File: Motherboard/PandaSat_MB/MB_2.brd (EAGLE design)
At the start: 93.9 x 89.2 mm, 164 parts, among them J1 503182-1852, J14 M023.5MM_LOCK, J15 M023.5MM_LOCK, J16 M023.5MM_LOCK, J2 10118194-0001LF, J3 DCJ0303, J4 BU-SMA-V, J5 BK-18650, K4 PE014006, Q1 IRLML2803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

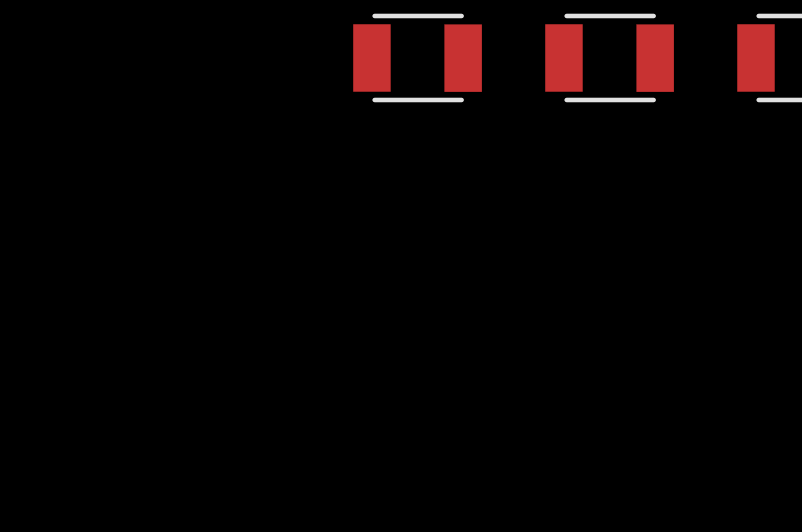
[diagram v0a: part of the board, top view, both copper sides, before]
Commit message: Added USB Bypass
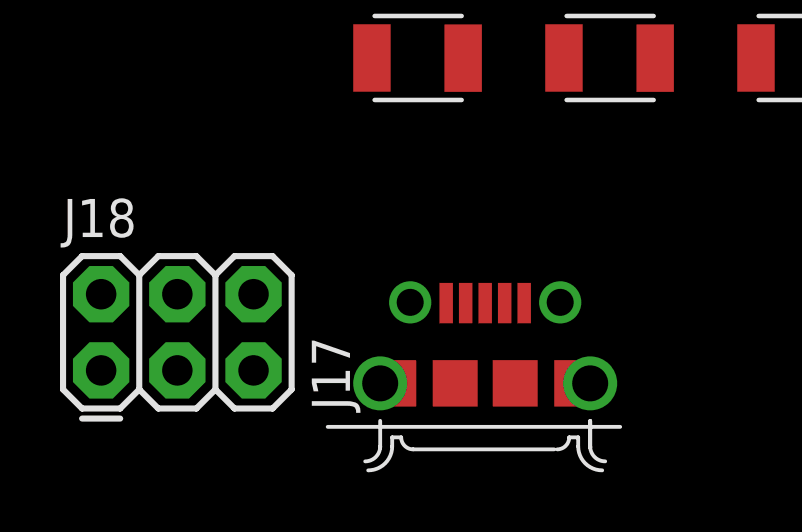
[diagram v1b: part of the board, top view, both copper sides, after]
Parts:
- added J17: 10118194-0001LF, 10118194-0001LF:FRAMATOME_10118194-0001LF
- added J18: (no value), SparkFun-Connectors:2X3
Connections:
- new net N$22: J17.3, J18.2
- new net N$40: J17.2, J18.4
- new net N$42: J17.1, J18.1
- new net N$57: J17.5, J18.5
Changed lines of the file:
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@@
 <attribute name="VALUE" x="-223.7434" y="-21.4674" size="1" layer="27"/>
+</element>
+<element name="J17" library="10118194-0001LF" package="FRAMATOME_10118194-0001LF" value="10118194-0001LF" x="-218.0082" y="-29.4132" smashed="yes">
+<attribute name="AVAILABILITY" value="Warning" x="-218.0082" y="-29.4132" size="1.778" layer="27" display="off"/>
+<attribute name="DESCRIPTION" value=" Micro Usb, 2.0 Type b, Rcpt, Smt " x="-218.0082" y="-29.4132" size="1.778" layer="27" display="off"/>
+<attribute name="MF" value="Amphenol" x="-218.0082" y="-29.4132" size="1.778" layer="27" display="off"/>
+<attribute name="MP" value="10118194-0001LF" x="-218.0082" y="-29.4132" size="1.778" layer="27" display="off"/>
+<attribute name="NAME" x="-222.5159" y="-30.314740625" size="1.27218125" layer="25" rot="R90"/>
+<attribute name="PACKAGE" value="None" x="-218.0082" y="-29.4132" size="1.778" layer="27" display="off"/>
+<attribute name="PRICE" value="0.26 USD" x="-218.0082" y="-29.4132" size="1.778" layer="27" display="off"/>
+<attribute name="VALUE" x="-212.099059375" y="-29.313046875" size="1.271959375" layer="27" rot="R90"/>
+</element>
+<element name="J18" library="SparkFun-Connectors" package="2X3" value="" x="-230.8098" y="-28.9814" smashed="yes">
+<attribute name="NAME" x="-232.0798" y="-24.5364" size="1.27" layer="25" ratio="10"/>
+<attribute name="VALUE" x="-232.0798" y="-32.1564" size="1.27" layer="27"/>
 </element>
 </elements>
@@
 <wire x1="-51.665" y1="32.451" x2="-212.3426" y2="-18.5724" width="0" layer="19" extent="1-1"/>
 </signal>
+<signal name="N$22">
+<contactref element="J17" pad="3"/>
+<contactref element="J18" pad="2"/>
+<wire x1="-230.8098" y1="-26.4414" x2="-218.0082" y2="-26.7382" width="0" layer="19" extent="1-1"/>
+</signal>
+<signal name="N$40">
+<contactref element="J17" pad="2"/>
+<contactref element="J18" pad="4"/>
+<wire x1="-218.6582" y1="-26.7382" x2="-228.2698" y2="-26.4414" width="0" layer="19" extent="1-1"/>
+</signal>
+<signal name="N$42">
+<contactref element="J17" pad="1"/>
+<contactref element="J18" pad="1"/>
+<wire x1="-230.8098" y1="-28.9814" x2="-219.3082" y2="-26.7382" width="0" layer="19" extent="1-1"/>
+</signal>
+<signal name="N$57">
+<contactref element="J17" pad="5"/>
+<contactref element="J18" pad="5"/>
+<wire x1="-216.7082" y1="-26.7382" x2="-225.7298" y2="-28.9814" width="0" layer="19" extent="1-1"/>
+</signal>
 </signals>

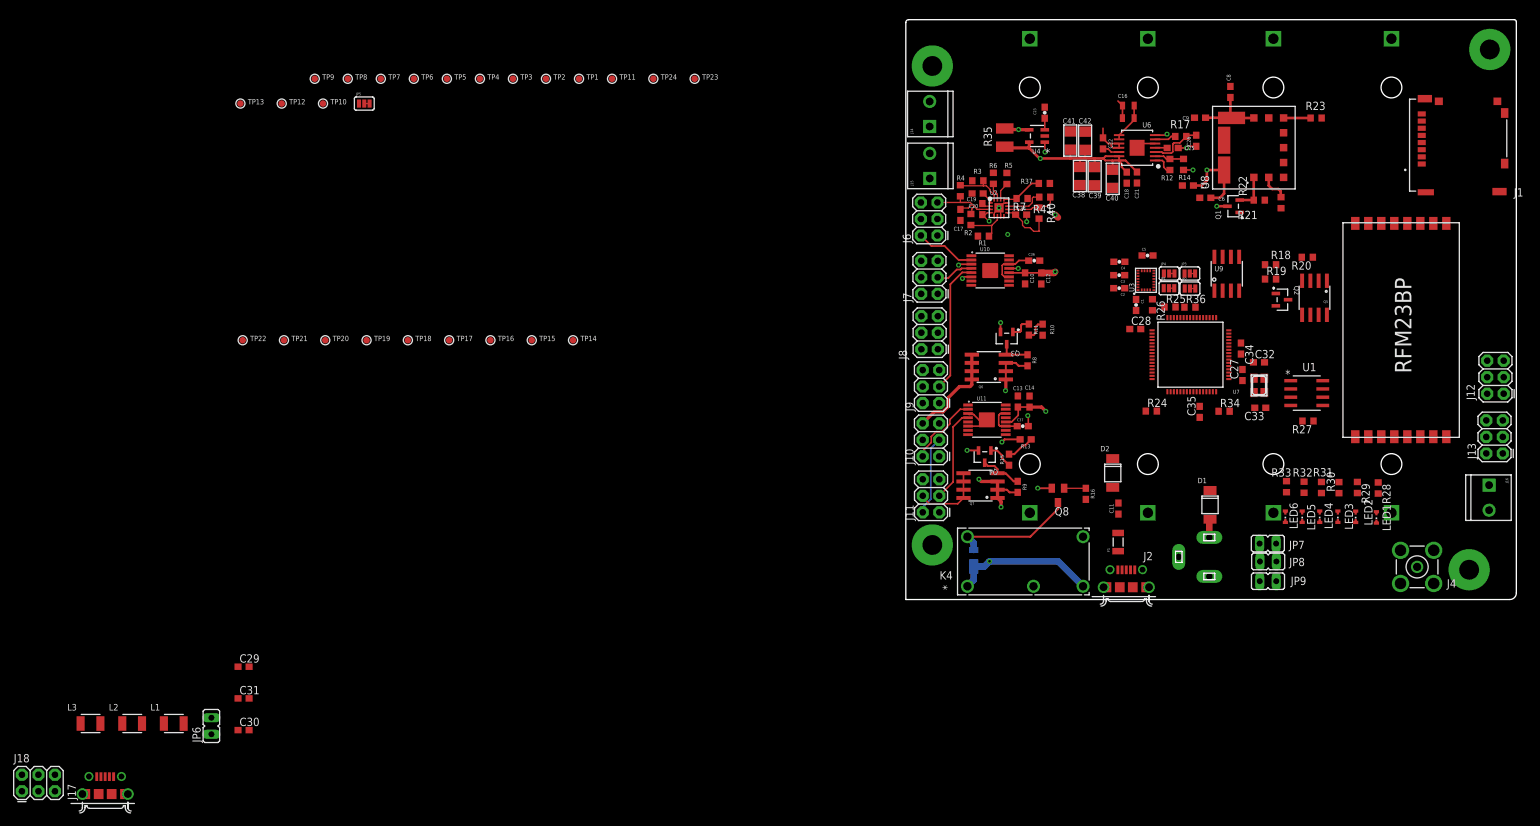
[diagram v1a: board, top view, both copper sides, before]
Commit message: Switched Barrel Jack to smd Changed Footprints for 2x3 conn to include casing Changed Hbridges to pair x&z instead of x&y fixed mislabeled net PL_PWR_EN -> PL_PWR_ENAB
Did all the signal routing, just need 5V and 3.3V
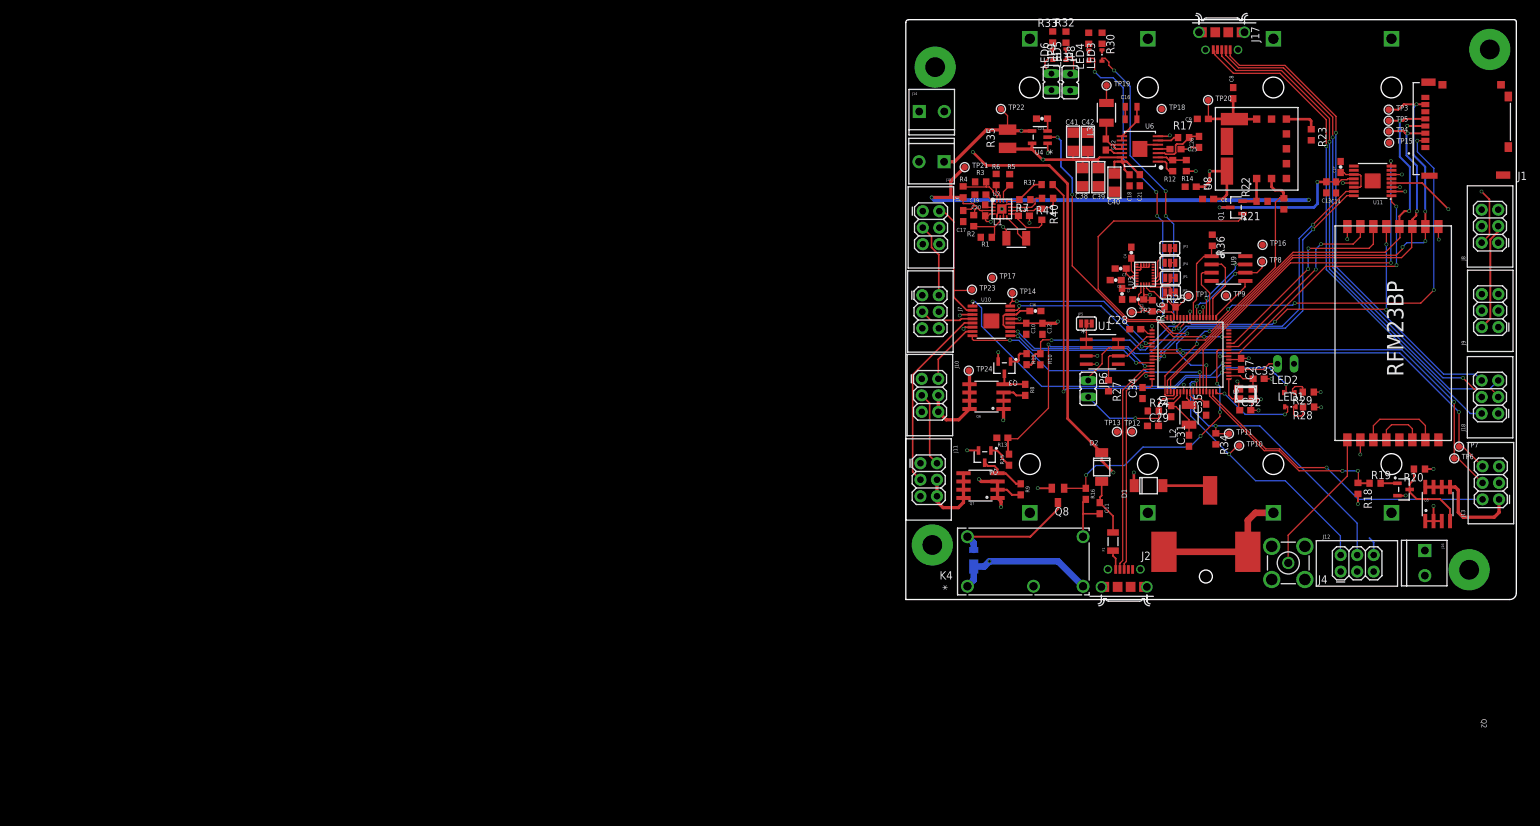
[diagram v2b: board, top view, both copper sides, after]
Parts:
- J10, J11, J12, J13, J18, J6, J7, J8, J9: device SparkFun-Connectors:2X3 -> pandasat:2X3
- J3: value DCJ0303 -> PJ-036AH-SMT-TRSMD; device maholli:DCJ0303 -> pandasat:BARRELJACK_5.0MMX2.1MM_SMD
- moved J18 234.3 mm to (-3.78, 29.1), turned to 90 degrees
- moved J17 207.9 mm to (-46.3, 87.7), turned to 180 degrees
- moved L3 182.3 mm to (-64.0, 75.4), turned to 90 degrees
- moved TP7 175.2 mm to (-9.81, 24.0)
- moved TP6 170.3 mm to (-10.5, 22.2)
- moved L2 169.3 mm to (-51.3, 28.9), turned to 90 degrees
- moved C30 150.8 mm to (-54.1, 29.5), turned to 90 degrees
- moved C31 150.7 mm to (-51.3, 24.9), turned to 90 degrees
- moved TP10 150.4 mm to (-43.6, 24.2)
- moved L1 149.5 mm to (-77.9, 56.1)
- moved TP5 145.0 mm to (-20.6, 74.1)
- moved C29 144.7 mm to (-56.9, 27.2)
- moved JP6 144.5 mm to (-66.8, 32.9), turned to 180 degrees
- moved TP9 144.0 mm to (-45.6, 47.2)
- moved TP13 143.9 mm to (-62.4, 26.3)
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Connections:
- net DXY_FAULT renamed DXZ_FAULT
- net DZ_FAULT renamed DY_FAULT
- net MXY_EN renamed MXZ_EN
- net MZ_EN renamed MY_EN
- removed net N$57: J17.5, J18.5
- removed net PL_PWR_EN: U7.62
- new net N$59: J16.1, J3.P$2, J3.P$3, J5.1, J5.2
- new net N$63: J7.6
- new net N$64: J7.4
- new net N$65: J8.6
- new net N$66: J8.4
- new net N$67: J9.6
- new net N$68: J9.4
- net MINY_1: now also U11.16; no longer U10.9
- net MINY_2: now also U11.15; no longer U10.10
- net MINZ_1: now also U10.9; no longer U11.16
- net MINZ_2: now also U10.10; no longer U11.15
- net MOY_1: now also U11.2; no longer U10.7
- net MOY_2: now also U11.4; no longer U10.5
- net MOZ_1: now also U10.7; no longer U11.2
- net MOZ_2: now also U10.5; no longer U11.4
- net N$22: now also J18.5; no longer J18.2
- net N$30: now also J17.2, J18.3; no longer J16.1, J3.2, J3.3, J5.1, J5.2
- net N$32: now also J3.P$1; no longer J3.1
- net N$40: now also J17.1, J18.6; no longer J17.2, J18.4
- net N$42: now also J17.5, J18.2; no longer J17.1, J18.1
- net PL_PWR_ENAB: now also U7.62
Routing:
- net VSOLAR: track 63.3 -> 172.0 mm, vias 0 -> 2
- net N$22: track 0.00 -> 78.8 mm, vias 0 -> 1
- net SPI_MISO: track 0.00 -> 78.5 mm, vias 0 -> 4
- net N$42: track 0.00 -> 78.3 mm, vias 0 -> 1
- net VBATT_IN: track 37.6 -> 113.4 mm, vias 0 -> 3
- net N$40: track 0.00 -> 73.9 mm, vias 0 -> 1
- net SPI_MOSI: track 0.00 -> 71.8 mm, vias 0 -> 2
- net SPI_SCK: track 0.00 -> 70.2 mm, vias 0 -> 2
- net SPI_CS_SD: track 0.00 -> 66.2 mm, vias 0 -> 4
- net PL_UART_TX: track 0.00 -> 64.4 mm, vias 0 -> 2
- net 5V_EN: track 0.00 -> 61.5 mm, vias 0 -> 2
- net PL_UART_RX: track 0.00 -> 61.2 mm, vias 0 -> 2
- net N$56: track 0.00 -> 59.2 mm, vias 0 -> 2
- net DY_FAULT: track 0.00 -> 57.3 mm, vias 0 -> 2
- net I_BATT: track 0.00 -> 50.9 mm, vias 0 -> 4
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
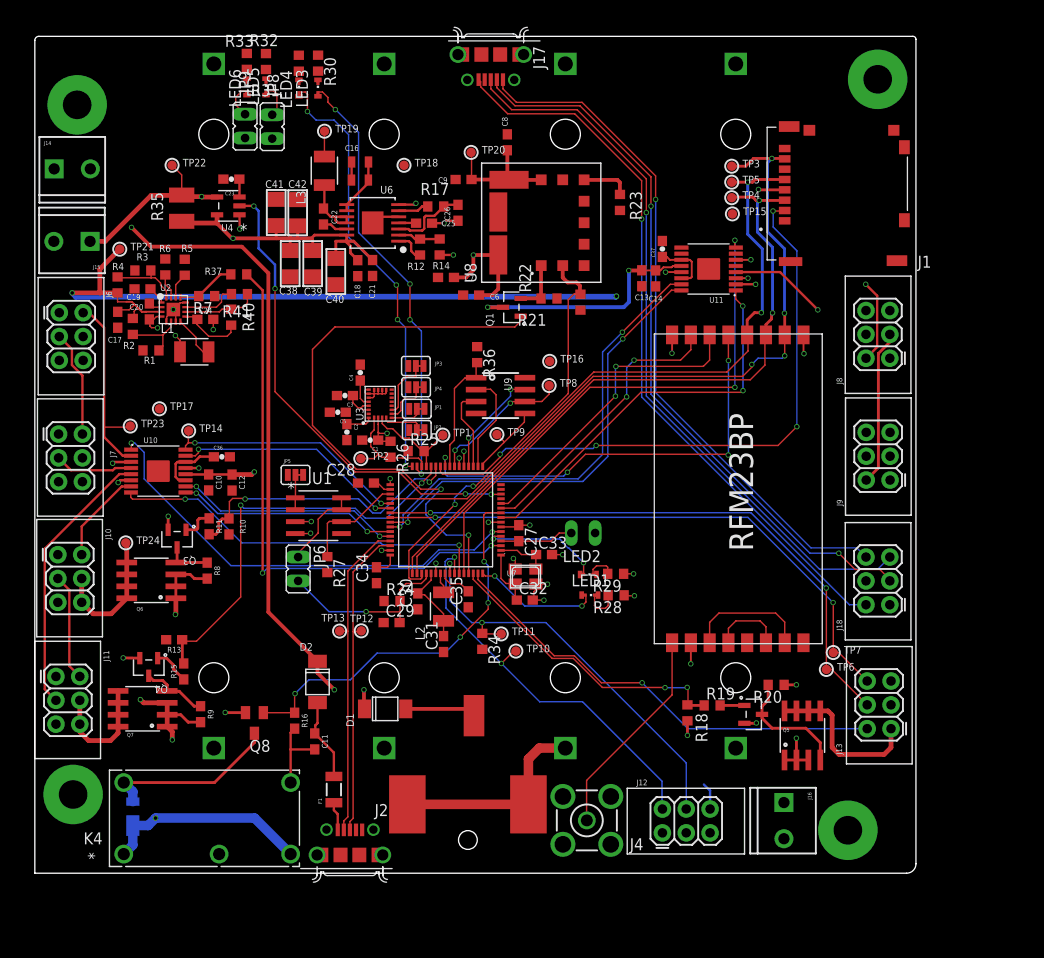
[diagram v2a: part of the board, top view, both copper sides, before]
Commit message: Finished?!? Rev  1 Routing - DRC < 50 Messages
Also Added Grnd and Power planes

Need to Fix LED foot print

Fix Weird VBatt Node
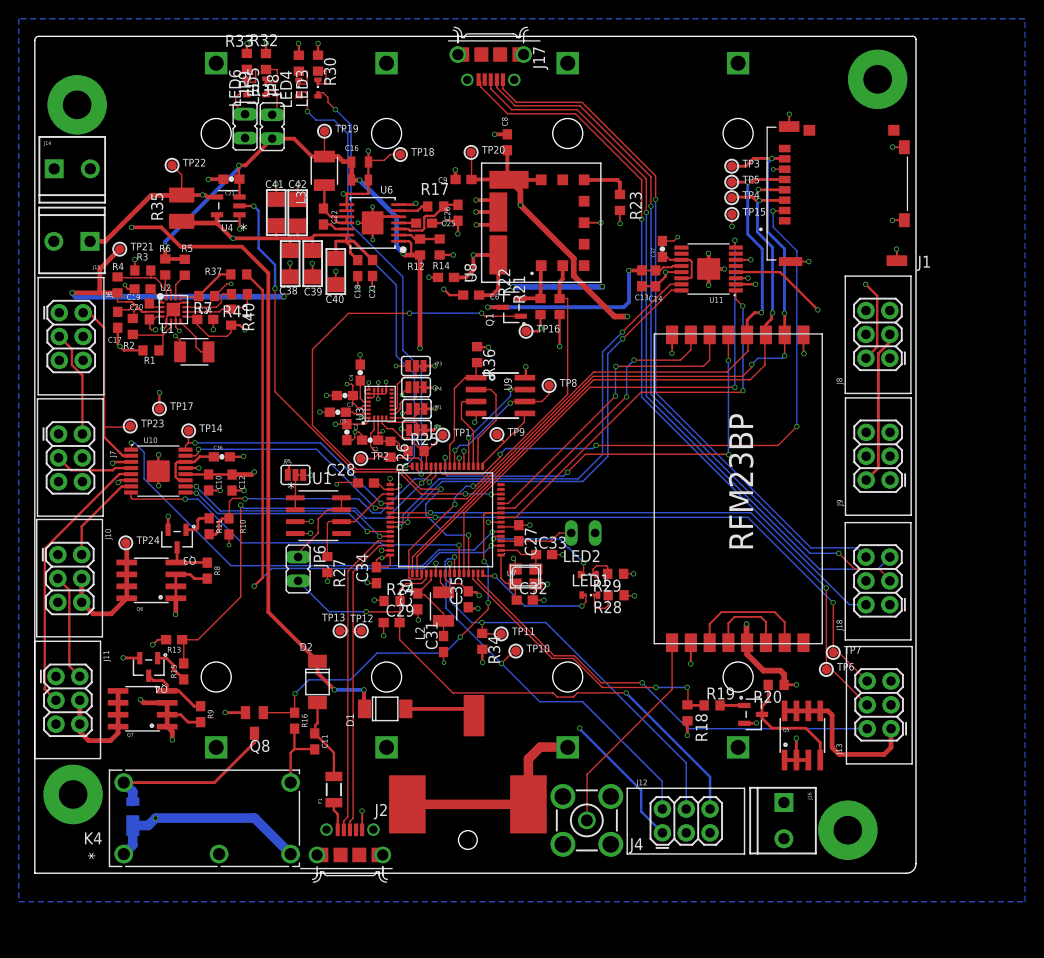
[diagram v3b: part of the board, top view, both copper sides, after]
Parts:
- moved TP16 4.07 mm to (-42.5, 58.2)
- moved R22 2.27 mm to (-39.0, 60.9)
- moved R21 1.25 mm to (-41.0, 60.9), turned to 90 degrees
- moved TP18 1.20 mm to (-55.9, 77.1)
- moved J5 0.27 mm to (-47.8, 50.4)
- moved TP15 0.07 mm to (-20.6, 70.7)
- moved TP13 0.06 mm to (-62.4, 26.3)
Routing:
- net 3.3V: track 35.1 -> 181.2 mm, vias 4 -> 26
- net GND: track 78.0 -> 200.4 mm, vias 32 -> 110
- net 5V: track 20.5 -> 131.0 mm, vias 2 -> 5
- net !RESET: track 22.5 -> 64.3 mm, vias 1 -> 2
- net N$41: track 143.8 -> 136.4 mm
- net N$49: track 0.00 -> 3.73 mm
- net N$56: track 59.2 -> 62.4 mm
- net N$50: track 0.00 -> 3.22 mm
- net N$48: track 0.00 -> 3.20 mm
- net N$47: track 0.00 -> 3.10 mm
- net VBATT: track 205.4 -> 208.4 mm, vias 6 -> 7
- net N$6: track 0.00 -> 2.51 mm
- net P_GOOD: track 45.2 -> 43.9 mm
- net N$37: track 7.82 -> 8.80 mm
- net QSPI_DATA[1]: track 9.93 -> 10.8 mm
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- added copper zone on layer 15, net 3.3V
- added copper zone on layer 16, net GND

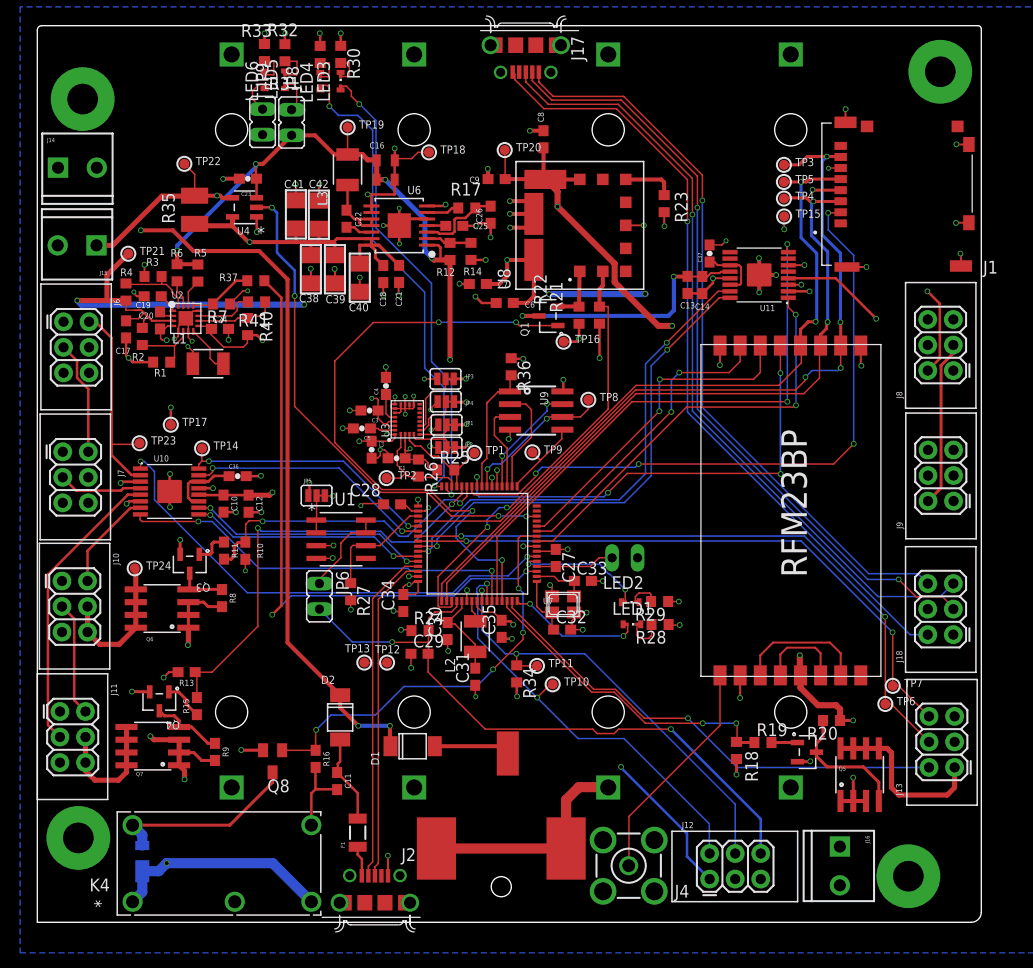
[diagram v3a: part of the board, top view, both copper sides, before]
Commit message: Fixed Mounting Hole misalignment and Passing DRC
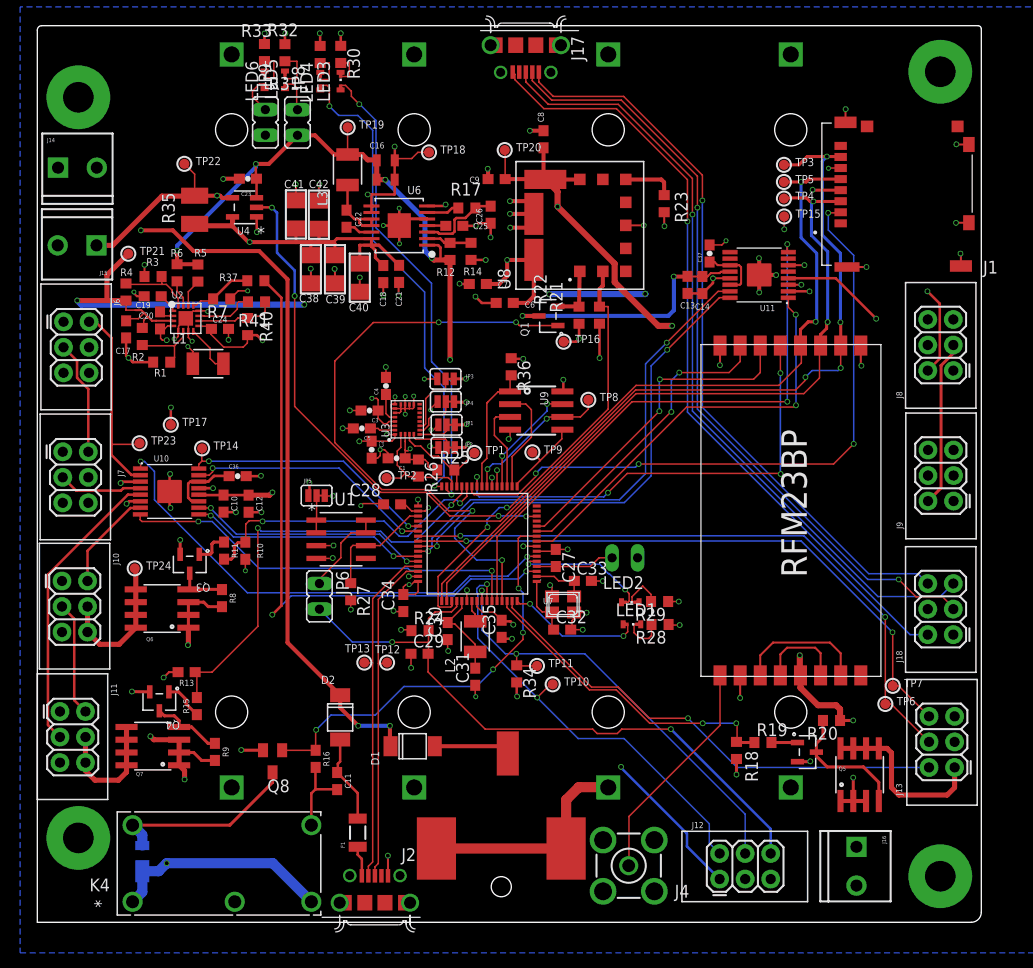
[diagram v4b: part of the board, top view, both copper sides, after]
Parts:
- moved J16 1.65 mm to (-13.4, 7.83)
- moved J12 0.99 mm to (-27.0, 4.80)
- moved JP8 0.58 mm to (-69.0, 80.0)
- moved R7 0.51 mm to (-76.5, 62.5)
- moved JP9 0.28 mm to (-72.2, 80.1)
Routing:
- net N$45: track 3.03 -> 4.19 mm
- net 5V: track 131.0 -> 130.0 mm
- net N$49: track 3.73 -> 4.43 mm
- net N$59: track 49.9 -> 50.6 mm
- net GND: track 200.4 -> 201.1 mm, vias 110 -> 111
- net N$50: track 3.22 -> 3.78 mm
- net N$48: track 3.20 -> 3.76 mm
- net VSOLAR: track 172.9 -> 172.4 mm
